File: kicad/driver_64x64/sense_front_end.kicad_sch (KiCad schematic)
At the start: 7 parts

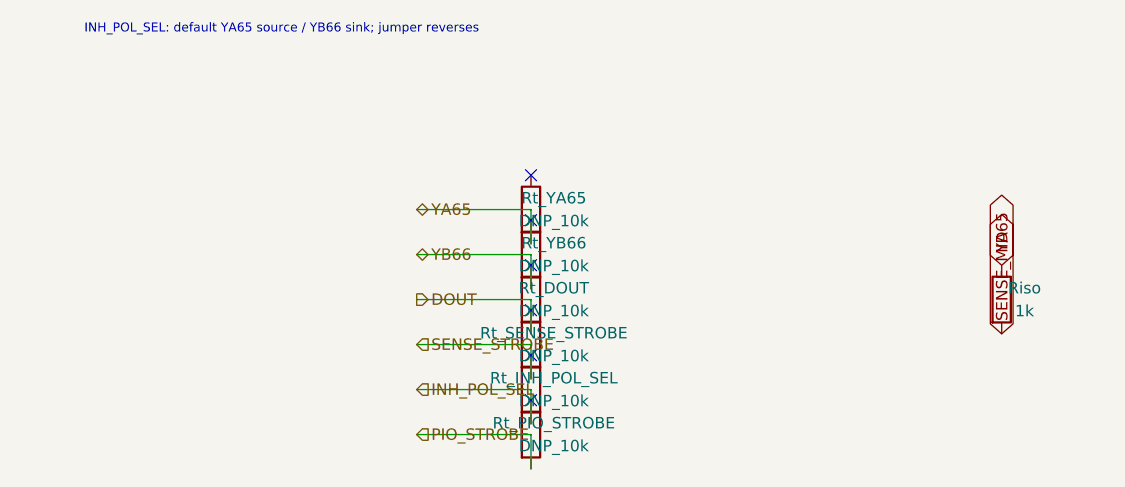
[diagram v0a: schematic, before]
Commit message: logical seperation into host and multiple decode/drive/steering boards
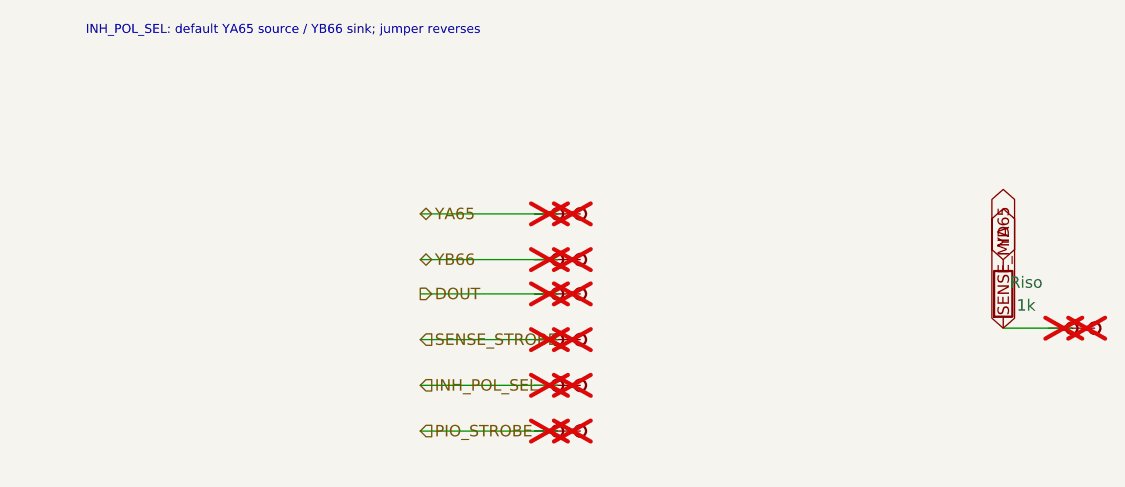
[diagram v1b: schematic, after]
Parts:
- removed Rt_DOUT, Rt_INH_POL_SEL, Rt_PIO_STROBE, Rt_SENSE_STROBE, Rt_YA65, Rt_YB66: DNP_10k, symbol Device:R
- added TP_DOUT, TP_DOUTb, TP_INH_POL_SEL, TP_INH_POL_SELb, TP_PIO_STROBE, TP_PIO_STROBEb, TP_SENSE_MID_90_17_43, TP_SENSE_MID_90_17_43b, TP_SENSE_STROBE, TP_SENSE_STROBEb, TP_YA65, TP_YA65b, TP_YB66, TP_YB66b: Stub, symbol CMR:Stub
- Riso: symbol Device:R -> CMR:R
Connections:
- net DOUT: now also TP_DOUT.1, TP_DOUTb.1
- net INH_POL_SEL: now also TP_INH_POL_SEL.1, TP_INH_POL_SELb.1
- net PIO_STROBE: now also TP_PIO_STROBE.1, TP_PIO_STROBEb.1
- net SENSE_MID: now also TP_SENSE_MID_90_17_43.1, TP_SENSE_MID_90_17_43b.1
- net SENSE_STROBE: now also TP_SENSE_STROBE.1, TP_SENSE_STROBEb.1
- net YA65: now also TP_YA65.1, TP_YA65b.1
- net YB66: now also TP_YB66.1, TP_YB66b.1
- no-connect marks 6 -> 0
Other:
- moved on the sheet: Riso
